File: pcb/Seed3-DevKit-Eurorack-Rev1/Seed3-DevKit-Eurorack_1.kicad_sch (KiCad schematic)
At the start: 70 parts, among them J7 USB4110GFA, U1 TL072, U12 CD4051B, U13 TL072, U14 USBLC6-2SC6, U15 TL072, U2 MCP6004

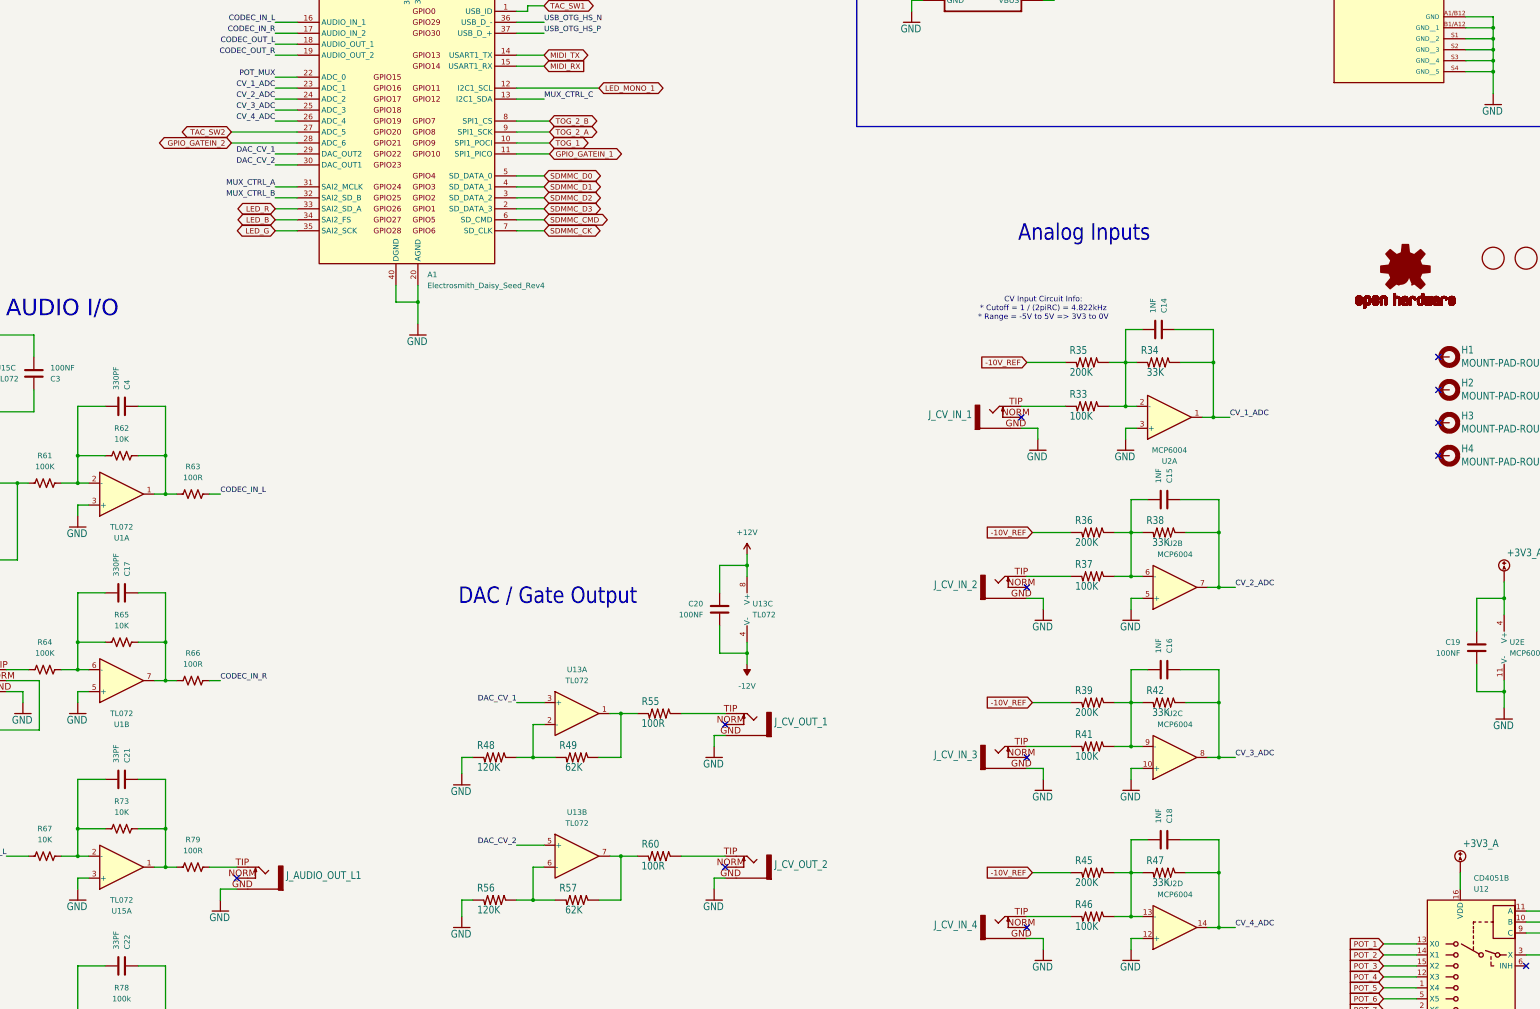
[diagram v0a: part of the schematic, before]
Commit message: finished routing board, fixed DRCs, and added cutout to PCB.
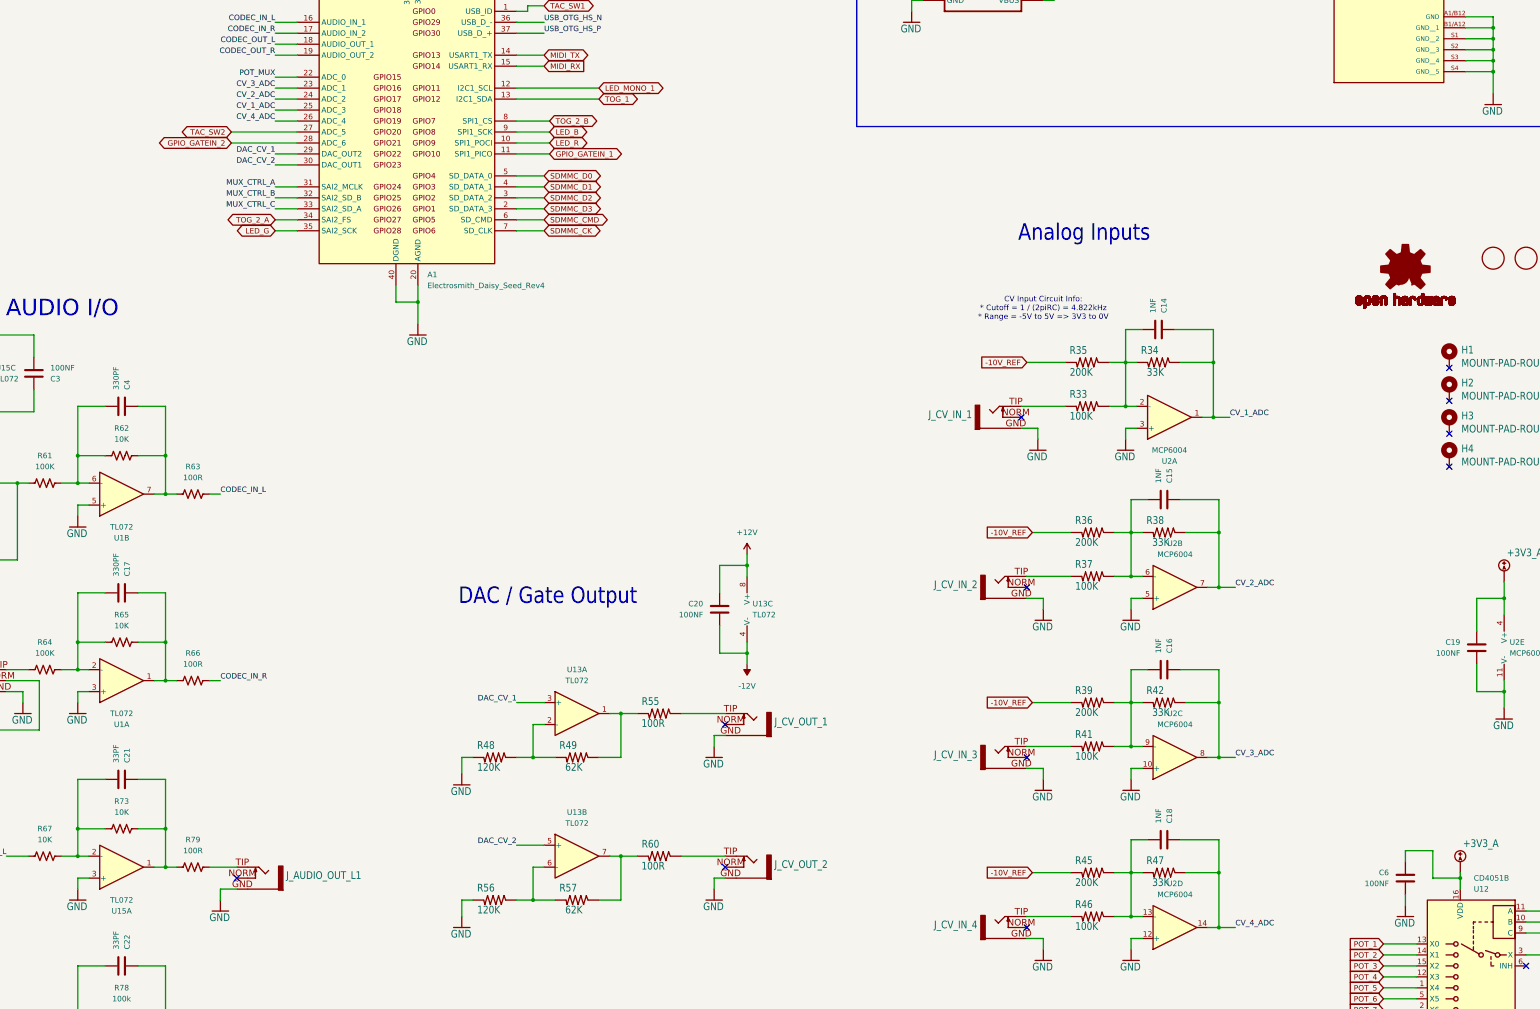
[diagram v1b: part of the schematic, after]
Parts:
- added C6: 100NF, Capacitor_SMD:C_0603_1608Metric, symbol Device:C
- H1, H2, H3, H4: footprint MountingHole:MountingHole_3.5mm_Pad -> MountingHole:MountingHole_3.2mm_M3_DIN965_Pad; symbol Seed3-Pedal-DevKit-Converted-eagle-import:MOUNT-PAD-ROUND3.5 -> Mechanical:MountingHole_Pad
- LOGO1: footprint parts-for-kicad:OSHW-LOGO-L_TEXT -> Symbol:OSHW-Logo2_14.6x12mm_SilkScreen
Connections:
- net +3V3_A: now also C6.1
- net CV_1_ADC: now also A1.25 (ADC_3); no longer A1.23 (ADC_1)
- net CV_3_ADC: now also A1.23 (ADC_1); no longer A1.25 (ADC_3)
- net GND: now also C6.2
- net LED_B: now also A1.9 (SPI1_SCK); no longer A1.34 (SAI2_FS)
- net LED_R: now also A1.10 (SPI1_POCI); no longer A1.33 (SAI2_SD_A)
- net MUX_CTRL_C: now also A1.33 (SAI2_SD_A); no longer A1.13 (I2C1_SDA)
- net TOG_1: now also A1.13 (I2C1_SDA); no longer A1.10 (SPI1_POCI)
- net TOG_2_A: now also A1.34 (SAI2_FS); no longer A1.9 (SPI1_SCK)
- net at C4.2, R61.1, R62.2: now also U1.6 (-); no longer U1.2 (-)
- net at C4.1, R62.1, R63.2: now also U1.7; no longer U1.1
- net at C17.2, R64.1, R65.2: now also U1.2 (-); no longer U1.6 (-)
- net at C17.1, R65.1, R66.2: now also U1.1; no longer U1.7
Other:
- moved on the sheet: U1A, U1B

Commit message: a lot of little silk changes.
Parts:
- H1, H2, H3, H4: footprint MountingHole:MountingHole_3.2mm_M3_DIN965_Pad -> shnsly:MNT_SLOT_M3_PLATED
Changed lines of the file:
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@@
 			)
 		)
-		(property "Footprint" "MountingHole:MountingHole_3.2mm_M3_DIN965_Pad"
+		(property "Footprint" "shnsly:MNT_SLOT_M3_PLATED"
 			(at 372.11 121.92 0)
 			(effects
@@
 			)
 		)
-		(property "Footprint" "MountingHole:MountingHole_3.2mm_M3_DIN965_Pad"
+		(property "Footprint" "shnsly:MNT_SLOT_M3_PLATED"
 			(at 372.11 129.54 0)
 			(effects
@@
 			)
 		)
-		(property "Footprint" "MountingHole:MountingHole_3.2mm_M3_DIN965_Pad"
+		(property "Footprint" "shnsly:MNT_SLOT_M3_PLATED"
 			(at 372.11 137.16 0)
 			(effects
@@
 			)
 		)
-		(property "Footprint" "MountingHole:MountingHole_3.2mm_M3_DIN965_Pad"
+		(property "Footprint" "shnsly:MNT_SLOT_M3_PLATED"
 			(at 372.11 114.3 0)
 			(effects
